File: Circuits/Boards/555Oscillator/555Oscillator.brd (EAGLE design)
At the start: 44.2 x 30.2 mm, 8 parts

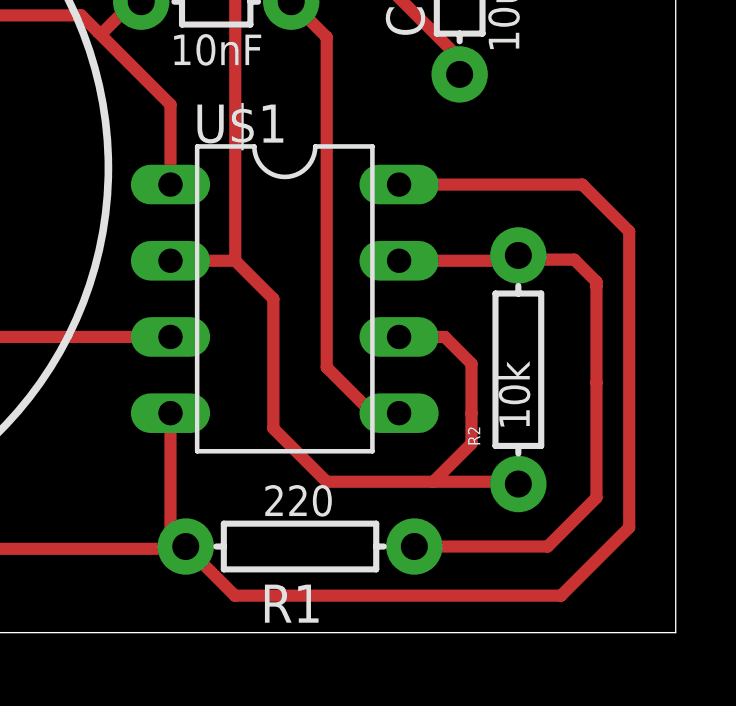
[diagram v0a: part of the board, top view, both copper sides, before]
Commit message: updated 555 board
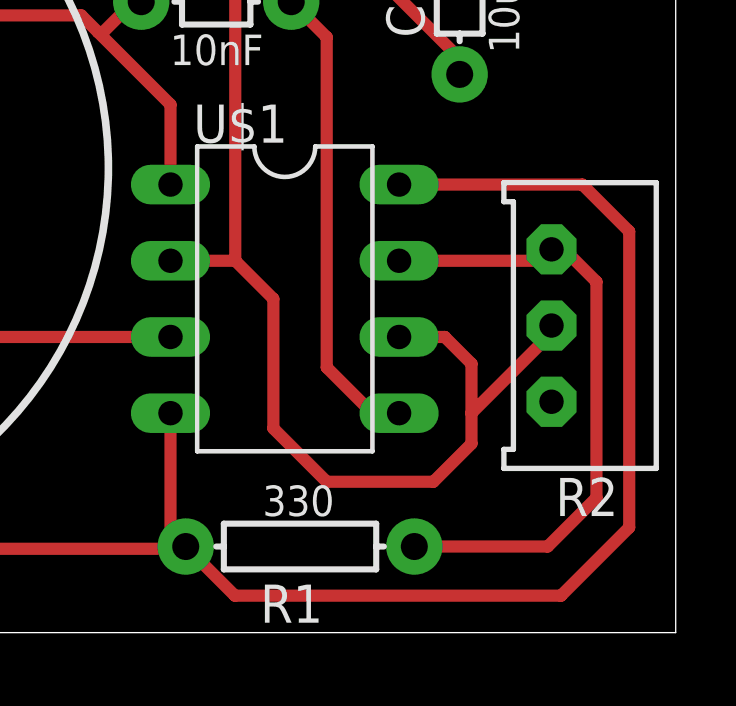
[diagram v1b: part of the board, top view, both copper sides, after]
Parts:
- R1: value 220 -> 330
- R2: value 10k -> (none); device HyTechDevices:AXIAL-0.3 -> HyTechDevices:TRIMPOT_3296
- moved R2 2.79 mm to (41.3, 10.5)
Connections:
- net N$13: now also R2.2; no longer R2.P$1
- net N$3: now also R2.1; no longer R2.P$2
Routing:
- net N$13: track 43.5 -> 44.7 mm
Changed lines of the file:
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@@
 <?xml version="1.0" encoding="utf-8"?>
 <!DOCTYPE eagle SYSTEM "eagle.dtd">
-<eagle version="9.1.3">
+<eagle version="9.4.2">
 <drawing>
 <settings>
@@
 <attribute name="VALUE" x="28.3591" y="24.8793" size="1.27" layer="27" ratio="10"/>
 </element>
-<element name="R1" library="HyTechDevices" package="AXIAL-0.3" value="220" x="31.623" y="3.175" smashed="yes" rot="R180">
+<element name="R1" library="HyTechDevices" package="AXIAL-0.3" value="330" x="31.623" y="3.175" smashed="yes" rot="R180">
 <attribute name="NAME" x="32.385" y="1.905" size="1.27" layer="25" font="vector" rot="R180"/>
 <attribute name="VALUE" x="32.766" y="5.207" size="1.016" layer="21" font="vector" ratio="15" rot="R180"/>
 </element>
+<element name="R2" library="HyTechDevices" package="TRIMPOT_3296" value="" x="41.275" y="10.541" smashed="yes" rot="R90">
+<attribute name="NAME" x="42.2275" y="5.461" size="1.27" layer="25" ratio="12" rot="R180"/>
+<attribute name="VALUE" x="38.1" y="6.731" size="1.27" layer="27" ratio="12" rot="R90"/>
+</element>
 <element name="R3" library="HyTechDevices" package="AXIAL-0.3" value="330" x="33.274" y="27.1907" smashed="yes" rot="R180">
 <attribute name="NAME" x="33.274" y="25.9207" size="1.27" layer="25" font="vector" rot="R180"/>
@@
 </element>
 <element name="U$2" library="HyTechDevices" package="CR-2450/G1AN" value="CR-2450/G1AN" x="12.7889" y="15.7988" smashed="yes" rot="R180"/>
-<element name="R2" library="HyTechDevices" package="AXIAL-0.3" value="10k" x="38.9001" y="9.0678" rot="R90"/>
 </elements>
 <signals>
@@
 <signal name="N$3">
 <contactref element="U$1" pad="7"/>
+<contactref element="R2" pad="1"/>
 <contactref element="R1" pad="P$1"/>
+<wire x1="40.132" y1="13.081" x2="40.005" y2="13.081" width="0.3048" layer="16"/>
+<wire x1="40.5511" y1="12.954" x2="40.132" y2="12.954" width="0.4064" layer="1"/>
+<wire x1="40.005" y1="13.081" x2="40.132" y2="12.954" width="0.4064" layer="1"/>
+<wire x1="41.5036" y1="12.0015" x2="40.5511" y2="12.954" width="0.4064" layer="1"/>
 <wire x1="39.878" y1="3.175" x2="35.433" y2="3.175" width="0.4064" layer="1"/>
+<wire x1="34.925" y1="12.7" x2="39.624" y2="12.7" width="0.4064" layer="1"/>
+<wire x1="39.624" y1="12.7" x2="40.005" y2="13.081" width="0.4064" layer="1"/>
 <wire x1="39.878" y1="3.175" x2="41.5036" y2="4.8006" width="0.4064" layer="1"/>
-<wire x1="41.5036" y1="4.8006" x2="41.5036" y2="8.636" width="0.4064" layer="1"/>
-<contactref element="R2" pad="P$2"/>
-<wire x1="41.5036" y1="8.636" x2="41.5036" y2="11.8491" width="0.4064" layer="1"/>
-<wire x1="41.5036" y1="11.8491" x2="41.5036" y2="12.0015" width="0.4064" layer="1"/>
-<wire x1="41.5036" y1="11.8491" x2="41.5036" y2="12.0523" width="0.1524" layer="1"/>
-<wire x1="41.5036" y1="12.0015" x2="40.767" y2="12.7381" width="0.4064" layer="1"/>
-<wire x1="40.767" y1="12.7381" x2="39.0398" y2="12.7381" width="0.4064" layer="1"/>
-<wire x1="38.9001" y1="12.8778" x2="38.7223" y2="12.7" width="0.4064" layer="1"/>
-<wire x1="38.7223" y1="12.7" x2="34.925" y2="12.7" width="0.4064" layer="1"/>
-<wire x1="39.0398" y1="12.7381" x2="38.9001" y2="12.8778" width="0.4064" layer="1"/>
+<wire x1="41.5036" y1="4.8006" x2="41.5036" y2="12.0015" width="0.4064" layer="1"/>
 </signal>
 <signal name="N$8">
@@
 <contactref element="U$1" pad="6"/>
 <contactref element="C1" pad="P$1"/>
+<contactref element="R2" pad="2"/>
 <wire x1="27.305" y1="12.7" x2="29.464" y2="12.7" width="0.4064" layer="1"/>
 <wire x1="30.734" y1="11.43" x2="30.734" y2="7.112" width="0.4064" layer="1"/>
@@
 <wire x1="37.338" y1="9.271" x2="36.449" y2="10.16" width="0.4064" layer="1"/>
 <wire x1="37.338" y1="9.271" x2="37.338" y2="7.62" width="0.4064" layer="1"/>
+<wire x1="40.005" y1="10.541" x2="40.005" y2="10.287" width="0.4064" layer="1"/>
+<wire x1="40.005" y1="10.287" x2="37.338" y2="7.62" width="0.4064" layer="1"/>
 <wire x1="36.9443" y1="18.9122" x2="36.9443" y2="19.4437" width="0.4064" layer="1"/>
 <wire x1="36.9443" y1="19.4437" x2="33.4518" y2="22.9362" width="0.4064" layer="1"/>
@@
 <wire x1="30.5562" y1="22.9362" x2="29.464" y2="21.844" width="0.4064" layer="1"/>
 <wire x1="29.464" y1="21.844" x2="29.464" y2="12.7" width="0.4064" layer="1"/>
-<contactref element="R2" pad="P$1"/>
-<wire x1="38.8239" y1="5.334" x2="36.068" y2="5.334" width="0.4064" layer="1"/>
-<wire x1="38.9001" y1="5.2578" x2="38.8239" y2="5.334" width="0.4064" layer="1"/>
 </signal>
 </signals>
